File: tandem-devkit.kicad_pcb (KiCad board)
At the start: 4 copper layers, 95.2 x 100 mm, 90 parts, among them J101 Conn_01x02, J102 QWIIC I2C Connector, J201 PCB Receptacle, J202 PCB Receptacle, J301 ConnectorLCDFrontLight, J302 FPC24(0.5MM), J303 FPC10(0.5MM), Q301 2N7002, Q302 2N7002, Q303 AO3401A, U201 AMS1117-ADJ_SOT223

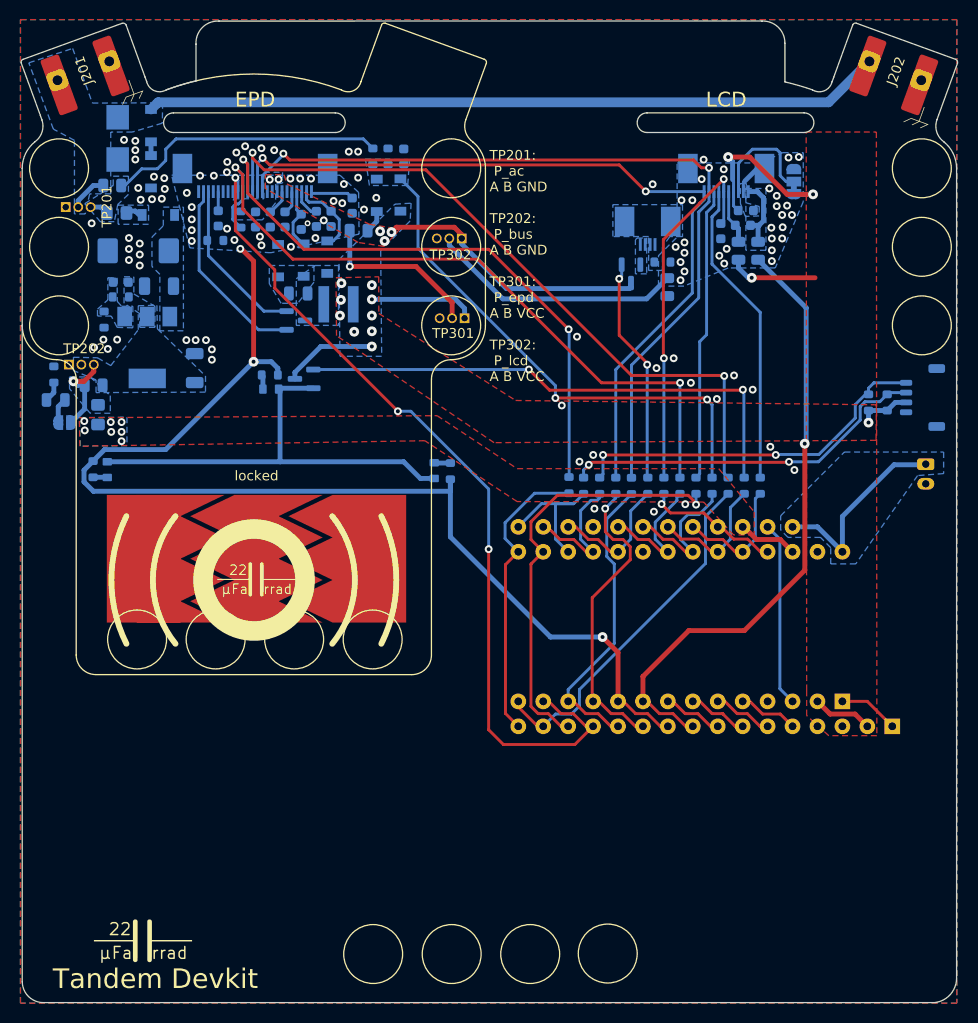
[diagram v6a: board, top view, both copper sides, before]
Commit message: Exchange brick-mount holes with actual footprint, connect holes to gnd
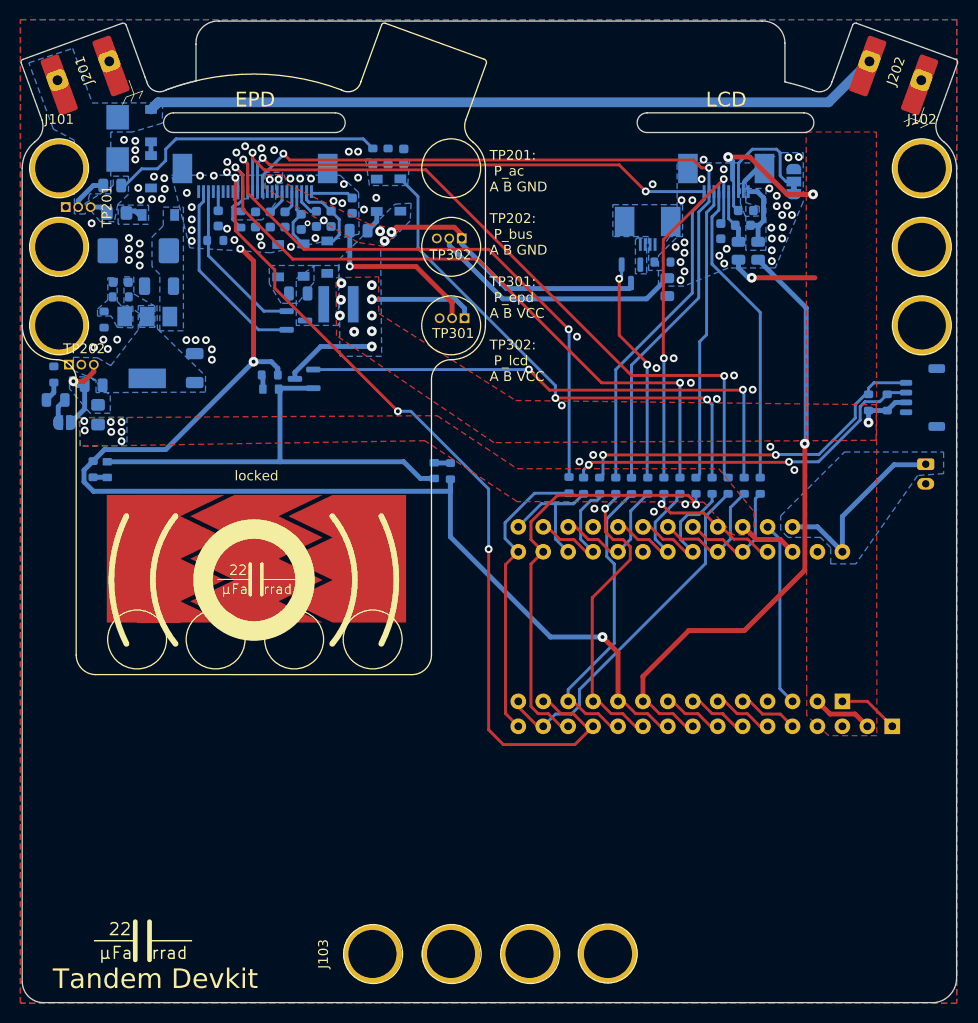
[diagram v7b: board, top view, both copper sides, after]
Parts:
- added J101: Conn_01x03, brick-mount:brick-1x3, F.Cu at (123.5, 43.2)
- added J102: Conn_01x03, brick-mount:brick-1x3, F.Cu at (211.4, 43.2)
- added J103: Conn_01x04, brick-mount:brick-1x4, F.Cu at (155.5, 123.2)
- renumbered C309 to C302, C307 to C306, C306 to C307, C310 to C309, C311 to C310, C302 to C311, J101 to J104, J102 to J105
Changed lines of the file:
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@@
   (net 31 "+BATT")
   (net 32 "Net-(C308-Pad2)")
-  (net 33 "Net-(C311-Pad1)")
+  (net 33 "Net-(C310-Pad1)")
   (net 34 "Net-(C312-Pad2)")
   (net 35 "Net-(D207-Pad1)")
@@
   (net 78 "unconnected-(A101-Pad20)")
   (net 79 "Net-(A101-Pad25)")
+  (footprint "brick-mount:brick-1x3" (layer "F.Cu")
+    (at 123.5456 43.1556)
+    (property "Sheetfile" "tandem-devkit.kicad_sch")
+    (property "Sheetname" "")
+    (attr through_hole)
+    (fp_text reference "J101" (at 0 -5) (layer "F.SilkS")
+      (effects (font (size 1 1) (thickness 0.15)))
+    )
+    (fp_text value "Conn_01x03" (at 0 21) (layer "F.Fab")
+      (effects (font (size 1 1) (thickness 0.15)))
+    )
+    (fp_line (start 4 -4) (end 4 20) (layer "F.CrtYd") (width 0.12))
+    (fp_line (start -4 20) (end -4 -4) (layer "F.CrtYd") (width 0.12))
+    (fp_line (start 4 20) (end -4 20) (layer "F.CrtYd") (width 0.12))
+    (fp_line (start -4 -4) (end 4 -4) (layer "F.CrtYd") (width 0.12))
+    (pad "1" thru_hole circle locked (at 0 0) (size 6 6) (drill 4.9) (layers *.Cu *.Mask)
+      (net 2 "GND") (pinfunction "Pin_1") (pintype "passive"))
+    (pad "2" thru_hole circle locked (at 0 8) (size 6 6) (drill 4.9) (layers *.Cu *.Mask)
+      (net 2 "GND") (pinfunction "Pin_2") (pintype "passive"))
+    (pad "3" thru_hole circle locked (at 0 16) (size 6 6) (drill 4.9) (layers *.Cu *.Mask)
+      (net 2 "GND") (pinfunction "Pin_3") (pintype "passive"))
+  )
   (footprint "project-lib:TouchSlider-3_30x13mm-covered" locked (layer "F.Cu")
     (at 143.646278 82.923333)
@@
     (fp_arc (start 46.190086 -18.7) (mid 45.468607 -19.698053) (end 45.481298 -20.929488) (layer "Edge.Cuts") (width 0.05))
   )
+  (footprint "brick-mount:brick-1x4" (layer "F.Cu")
+    (at 155.4622 123.19 90)
+    (property "Sheetfile" "tandem-devkit.kicad_sch")
+    (property "Sheetname" "")
+    (attr through_hole)
+    (fp_text reference "J103" (at 0 -5 90) (layer "F.SilkS")
+      (effects (font (size 1 1) (thickness 0.15)))
+    )
+    (fp_text value "Conn_01x04" (at 0 29 90) (layer "F.Fab")
+      (effects (font (size 1 1) (thickness 0.15)))
+    )
+    (fp_line (start 4 28) (end -4 28) (layer "F.CrtYd") (width 0.12))
+    (fp_line (start 4 -4) (end 4 28) (layer "F.CrtYd") (width 0.12))
+    (fp_line (start -4 -4) (end 4 -4) (layer "F.CrtYd") (width 0.12))
+    (fp_line (start -4 28) (end -4 -4) (layer "F.CrtYd") (width 0.12))
+    (pad "1" thru_hole circle locked (at 0 0 90) (size 6 6) (drill 4.9) (layers *.Cu *.Mask)
+      (net 2 "GND") (pinfunction "Pin_1") (pintype "passive"))
+    (pad "2" thru_hole circle locked (at 0 8 90) (size 6 6) (drill 4.9) (layers *.Cu *.Mask)
+      (net 2 "GND") (pinfunction "Pin_2") (pintype "passive"))
+    (pad "3" thru_hole circle locked (at 0 16 90) (size 6 6) (drill 4.9) (layers *.Cu *.Mask)
+      (net 2 "GND") (pinfunction "Pin_3") (pintype "passive"))
+    (pad "4" thru_hole circle locked (at 0 24 90) (size 6 6) (drill 4.9) (layers *.Cu *.Mask)
+      (net 2 "GND") (pinfunction "Pin_4") (pintype "passive"))
+  )
   (footprint "project-lib:154_Epaper_Display" (layer "F.Cu")
     (at 143.472086 57.1465 180)
@@
     )
   )
+  (footprint "brick-mount:brick-1x3" (layer "F.Cu")
+    (at 211.4296 43.1556)
+    (property "Sheetfile" "tandem-devkit.kicad_sch")
+    (property "Sheetname" "")
+    (attr through_hole)
+    (fp_text reference "J102" (at 0 -5) (layer "F.SilkS")
+      (effects (font (size 1 1) (thickness 0.15)))
+    )
+    (fp_text value "Conn_01x03" (at 0 21) (layer "F.Fab")
+      (effects (font (size 1 1) (thickness 0.15)))
+    )
+    (fp_line (start -4 20) (end -4 -4) (layer "F.CrtYd") (width 0.12))
+    (fp_line (start 4 -4) (end 4 20) (layer "F.CrtYd") (width 0.12))
+    (fp_line (start 4 20) (end -4 20) (layer "F.CrtYd") (width 0.12))
+    (fp_line (start -4 -4) (end 4 -4) (layer "F.CrtYd") (width 0.12))
+    (pad "1" thru_hole circle locked (at 0 0) (size 6 6) (drill 4.9) (layers *.Cu *.Mask)
+      (net 2 "GND") (pinfunction "Pin_1") (pintype "passive"))
+    (pad "2" thru_hole circle locked (at 0 8) (size 6 6) (drill 4.9) (layers *.Cu *.Mask)
+      (net 2 "GND") (pinfunction "Pin_2") (pintype "passive"))
+    (pad "3" thru_hole circle locked (at 0 16) (size 6 6) (drill 4.9) (layers *.Cu *.Mask)
+      (net 2 "GND") (pinfunction "Pin_3") (pintype "passive"))
+  )
   (footprint "project-lib:shimano-hub-generator-connector" (layer "F.Cu")
     (at 208.756 33.227 -20)
@@
       (net 70 "unconnected-(J302-Pad4)") (pinfunction "Pin_4") (pintype "passive+no_connect"))
     (pad "5" smd rect (at -3.75 1.02) (size 0.3 1.3) (layers "B.Cu" "B.Paste" "B.Mask")
-      (net 33 "Net-(C311-Pad1)") (pinfunction "Pin_5") (pintype "passive"))
+      (net 33 "Net-(C310-Pad1)") (pinfunction "Pin_5") (pintype "passive"))
     (pad "6" smd rect (at -3.25 1.02) (size 0.3 1.3) (layers "B.Cu" "B.Paste" "B.Mask")
       (net 71 "unconnected-(J302-Pad6)") (pinfunction "Pin_6") (pintype "passive+no_connect"))
@@
     (property "Sheetname" "Display")
     (attr smd)
-    (fp_text reference "C307" (at 0 1.43 90) (layer "B.SilkS") hide
+    (fp_text reference "C306" (at 0 1.43 90) (layer "B.SilkS") hide
       (effects (font (size 1 1) (thickness 0.15)) (justify mirror))
     )
@@
     (property "Sheetname" "Display")
     (attr smd)
-    (fp_text reference "C302" (at 0 1.43) (layer "B.SilkS") hide
+    (fp_text reference "C311" (at 0 1.43) (layer "B.SilkS") hide
       (effects (font (size 1 1) (thickness 0.15)) (justify mirror))
     )
@@
     (property "Sheetname" "Display")
     (attr smd)
-    (fp_text reference "C311" (at 0 1.43 -270) (layer "B.SilkS") hide
+    (fp_text reference "C310" (at 0 1.43 -270) (layer "B.SilkS") hide
       (effects (font (size 1 1) (thickness 0.15)) (justify mirror))
     )
@@
     (fp_line (start -0.8 0.4) (end 0.8 0.4) (layer "B.Fab") (width 0.1))
     (pad "1" smd roundrect (at -0.775 0 270) (size 0.9 0.95) (layers "B.Cu" "B.Paste" "B.Mask") (roundrect_rratio 0.25)
-      (net 33 "Net-(C311-Pad1)") (pintype "passive"))
+      (net 33 "Net-(C310-Pad1)") (pintype "passive"))
     (pad "2" smd roundrect (at 0.775 0 270) (size 0.9 0.95) (layers "B.Cu" "B.Paste" "B.Mask") (roundrect_rratio 0.25)
       (net 41 "/EPD_CURRENT_SENSE") (pintype "passive"))
@@
     (property "Sheetname" "Display")
     (attr smd)
-    (fp_text reference "C309" (at 0 1.43 -270) (layer "B.SilkS") hide
+    (fp_text reference "C302" (at 0 1.43 -270) (layer "B.SilkS") hide
       (effects (font (size 1 1) (thickness 0.15)) (justify mirror))
     )
@@
     (property "Sheetname" "")
     (attr smd)
-    (fp_text reference "J102" (at -3.15 3.6 90) (layer "B.SilkS")
+    (fp_text reference "J105" (at -3.15 3.6 90) (layer "B.SilkS")
       (effects (font (size 1 1) (thickness 0.15)) (justify mirror))
     )
@@
     (property "Sheetname" "")
     (attr through_hole)
-    (fp_text reference "J101" (at 1 2.9 -270) (layer "B.SilkS")
+    (fp_text reference "J104" (at 1 2.9 -270) (layer "B.SilkS")
       (effects (font (size 1 1) (thickness 0.15)) (justify mirror))
     )
@@
     (property "Sheetname" "Display")
     (attr smd)
-    (fp_text reference "C310" (at 0 1.43 90) (layer "B.SilkS") hide
+    (fp_text reference "C309" (at 0 1.43 90) (layer "B.SilkS") hide
       (effects (font (size 1 1) (thickness 0.15)) (justify mirror))
     )
@@
     (property "Sheetname" "Display")
     (attr smd)
-    (fp_text reference "C306" (at 0 1.43) (layer "B.SilkS") hide
+    (fp_text reference "C307" (at 0 1.43) (layer "B.SilkS") hide
       (effects (font (size 1 1) (thickness 0.15)) (justify mirror))
     )

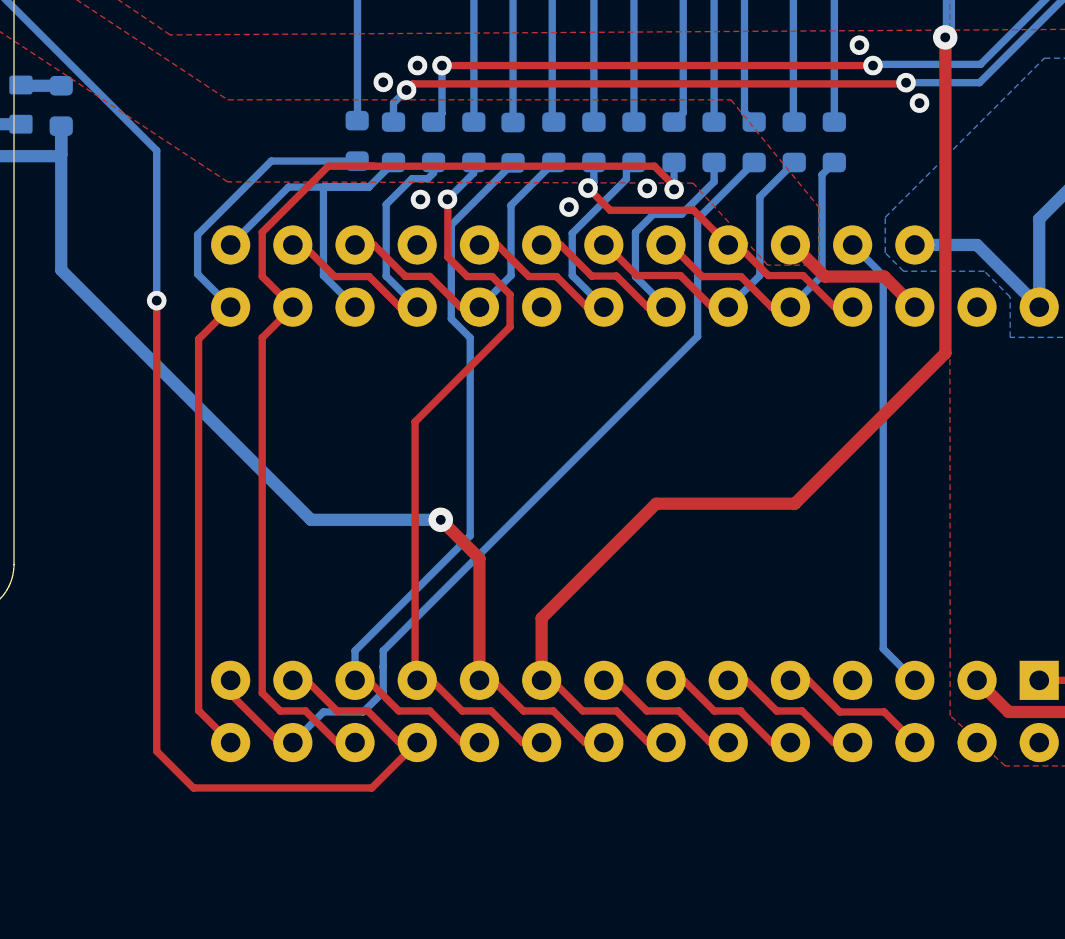
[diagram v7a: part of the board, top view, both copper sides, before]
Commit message: connect everything except the capacitive touch sensors
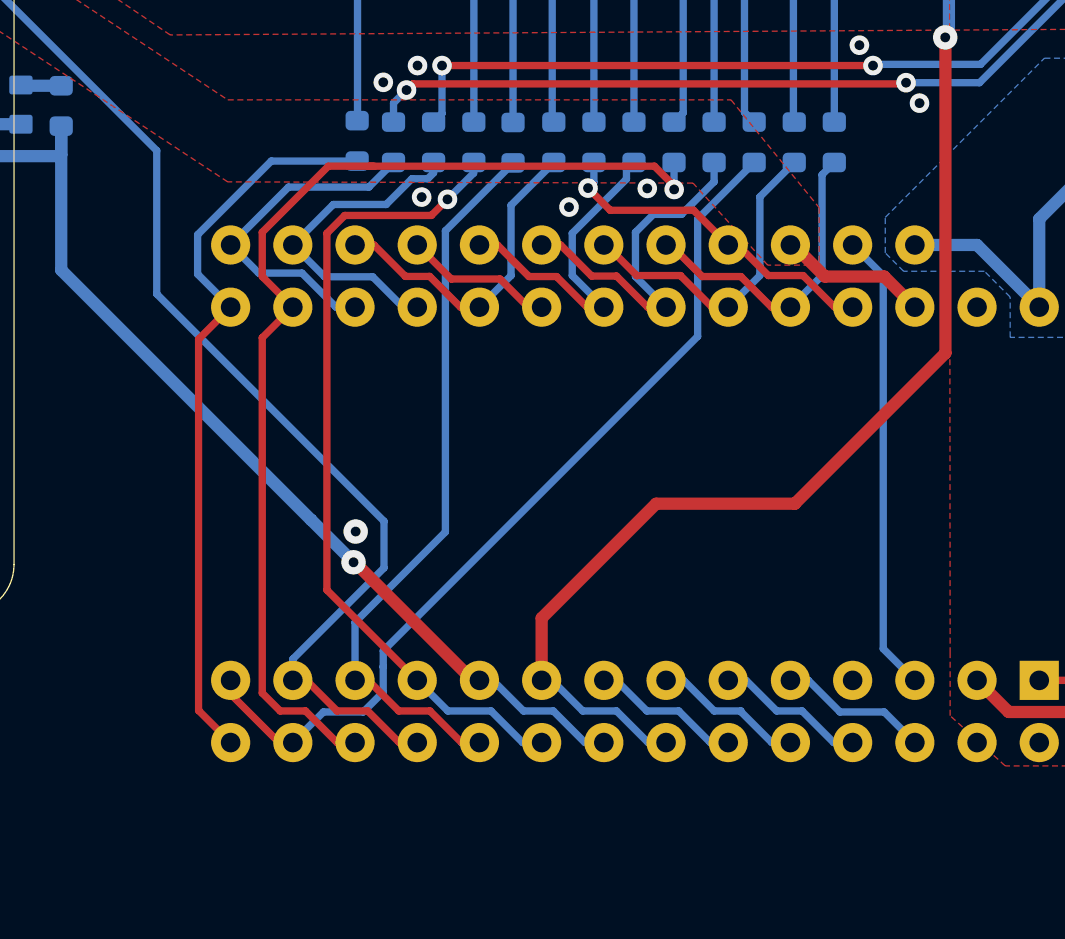
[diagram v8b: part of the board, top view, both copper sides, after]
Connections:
- A101 pad 20: unconnected-(A101-Pad20) -> Net-(A101-Pad20)
- A102 pad 20: unconnected-(A101-Pad20) -> Net-(A101-Pad20)
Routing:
- net /~{EPD_BUSY}: track 87.4 -> 77.9 mm, vias 3 -> 2
- net Net-(A101-Pad20): track 0.00 -> 6.13 mm
- net Net-(A101-Pad11): track 31.0 -> 34.0 mm
- net /EPD_CURRENT_SENSE: track 133.7 -> 130.8 mm
- net Net-(A101-Pad17): track 15.3 -> 14.2 mm
- net Net-(A101-Pad12): track 30.6 -> 30.0 mm
- net GND: vias 56 -> 57
